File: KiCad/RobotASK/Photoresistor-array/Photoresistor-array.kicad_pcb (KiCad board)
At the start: 2 copper layers, 100 x 15 mm, 10 parts, among them J1 Conn_01x04_Pin, J2 Conn_01x02_Pin

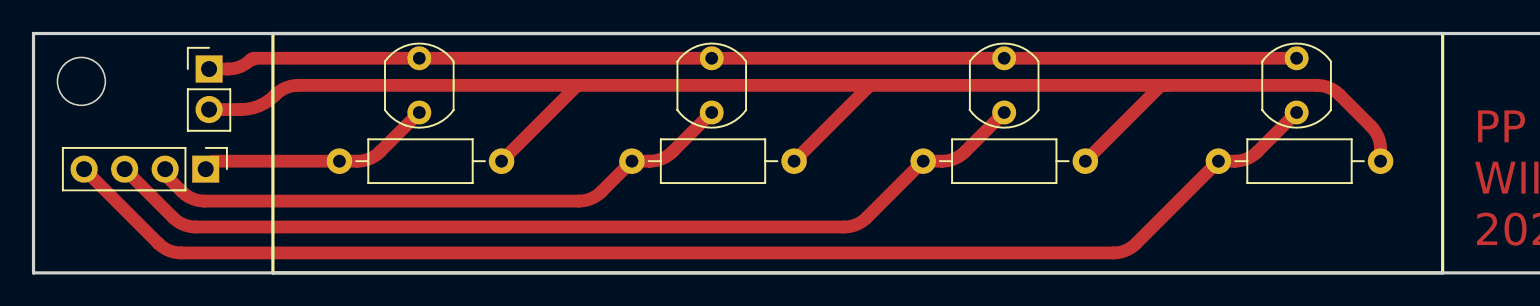
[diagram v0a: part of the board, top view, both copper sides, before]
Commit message: Edit pcb layers
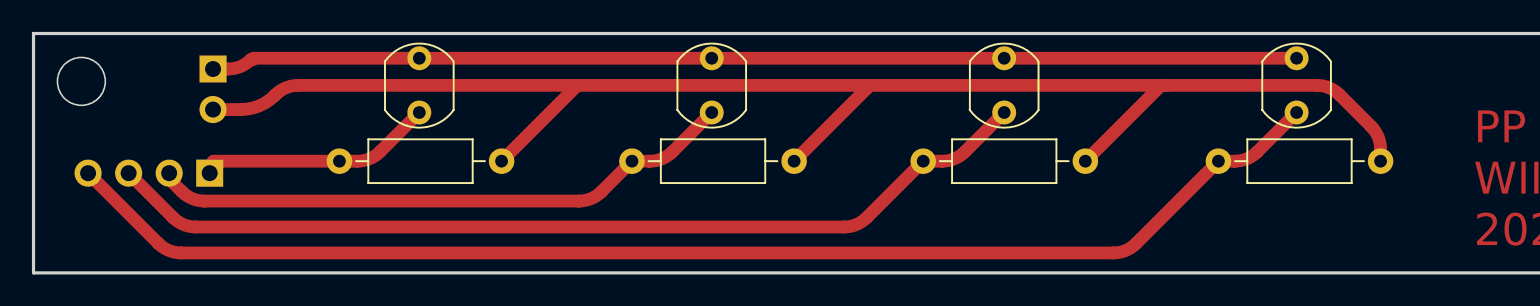
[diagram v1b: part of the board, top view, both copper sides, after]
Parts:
- J1, J2: moved to B.Cu
- moved J1 0.35 mm to (96.0, 58.8), turned to 90 degrees
- moved J2 0.25 mm to (96.2, 52.2), turned to 180 degrees

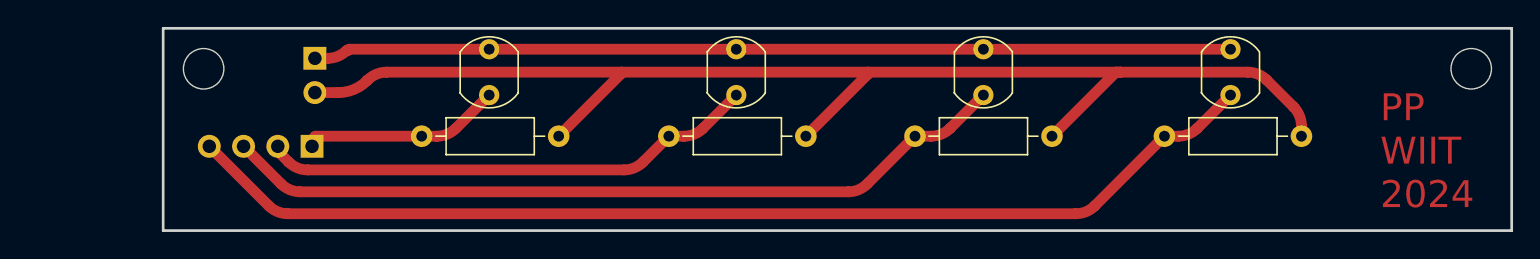
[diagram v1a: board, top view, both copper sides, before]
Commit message: Płytka fotorezystorów przedłużona aby piny były na dole
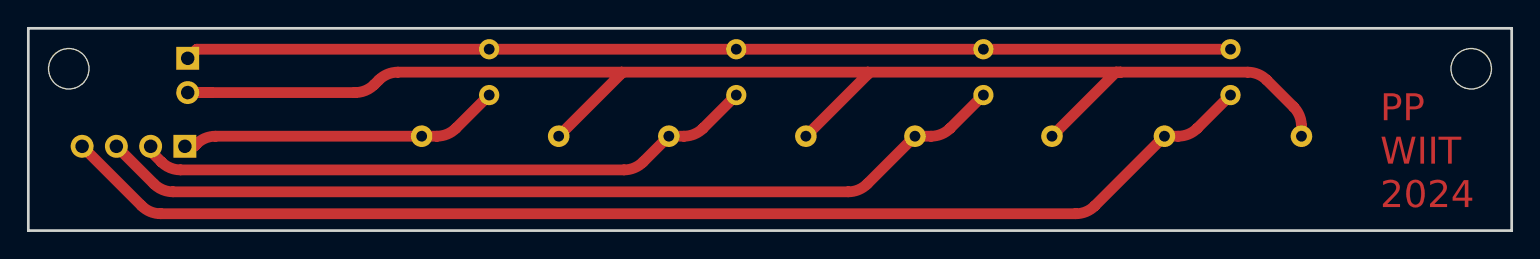
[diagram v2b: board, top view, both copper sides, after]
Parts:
- R1, R2, R3, R4, R5, R6, R7, R8: moved to B.Cu
- moved J1 9.43 mm to (86.6, 58.8)
- moved J2 9.43 mm to (86.8, 52.2)
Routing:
- net GND: track 96.9 -> 108.1 mm
- net PH1: track 37.3 -> 46.7 mm
- net PH2: track 59.3 -> 68.7 mm
- net PH3: track 81.5 -> 90.9 mm
- net +5V: track 68.3 -> 77.6 mm
- net PH0: track 14.8 -> 23.9 mm
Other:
- board size 100 x 15 mm -> 110 x 15 mm

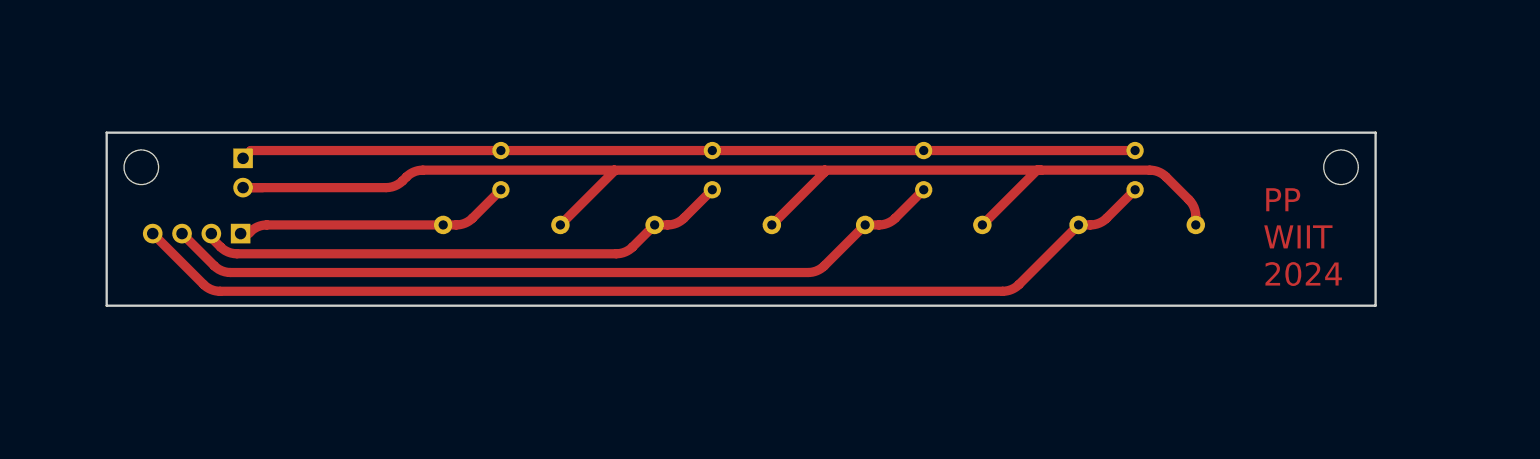
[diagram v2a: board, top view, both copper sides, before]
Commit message: Widen all possible traces, fill edge cuts layer, widen photoresistor PCB by 2mm
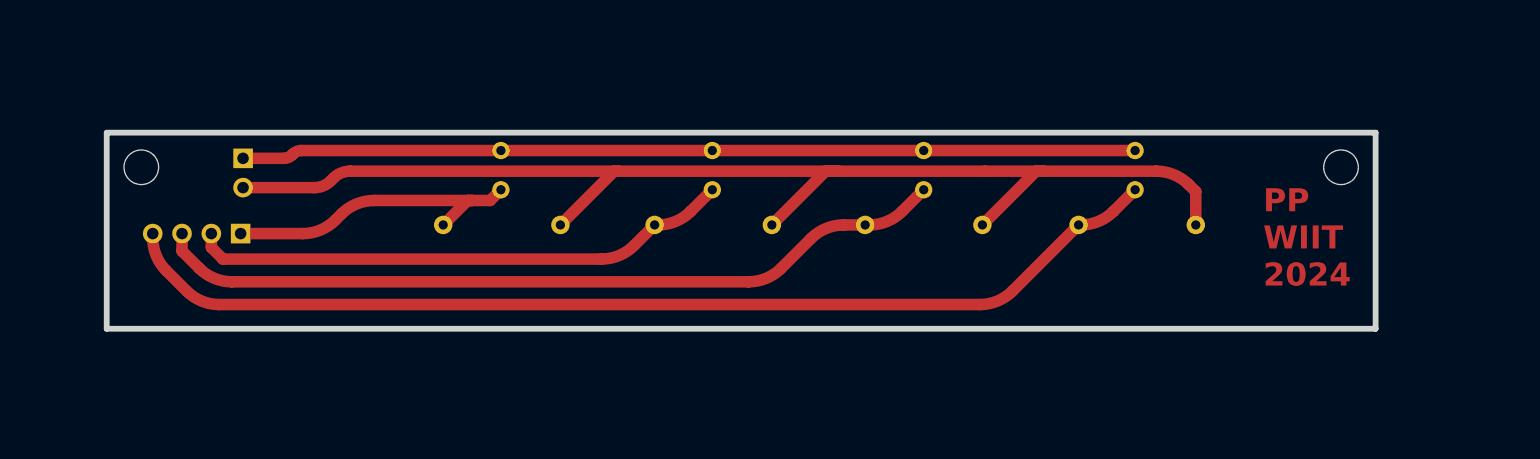
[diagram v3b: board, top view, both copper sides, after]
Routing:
- net PH0: track 23.9 -> 27.1 mm
- net PH3: track 90.9 -> 92.3 mm
- net PH2: track 68.7 -> 69.4 mm
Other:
- board size 110 x 15 mm -> 110 x 17 mm

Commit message: Poprawki kodu, zwiększenie otworów na komponenty na 1mm, nowe wydruki do termotransferu i nawiercania otworów, poukładanie nieaktualnych wydruków UV
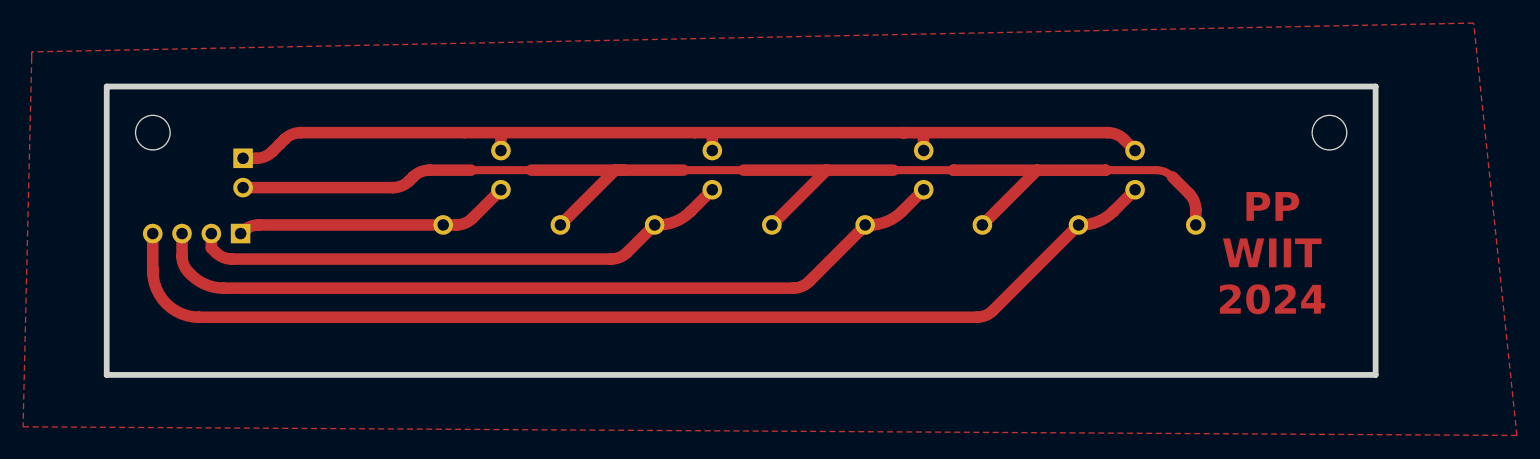
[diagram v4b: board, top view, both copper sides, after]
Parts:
- R1, R2, R3, R4: footprint Resistor_THT:R_Axial_DIN0207_L6.3mm_D2.5mm_P10.16mm_Horizontal -> Library:R_Axial_DIN0207_L6.3mm_D2.5mm_P10.16mm_Horizontal
- R5, R6, R7, R8: footprint OptoDevice:R_LDR_5.1x4.3mm_P3.4mm_Vertical -> Library:R_LDR_5.1x4.3mm_P3.4mm_Vertical
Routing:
- net +5V: track 77.5 -> 83.6 mm
- net PH0: track 27.1 -> 23.9 mm
- net PH3: track 92.3 -> 95.2 mm
- net PH2: track 69.4 -> 71.7 mm
- net GND: track 107.9 -> 106.9 mm
- added copper zone on F.Cu, net GND
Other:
- board size 110 x 17 mm -> 110 x 25 mm

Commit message: renders
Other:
- board text added: "+5V"
- board text added: "GND"
- board text added: "P0"
- board text added: "P1"
- board text added: "P2"
- board text added: "P3"
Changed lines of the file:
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@@
 		(0 "F.Cu" signal)
 		(31 "B.Cu" signal)
+		(36 "B.SilkS" user "B.Silkscreen")
 		(41 "Cmts.User" user "User.Comments")
 		(44 "Edge.Cuts" user)
@@
 			(layer "dielectric 1"
 				(type "prepreg")
-				(thickness 1)
+				(color "#633C00F2")
+				(thickness 1 locked)
 				(material "FR4")
 				(epsilon_r 4.5)
@@
 				(thickness 0.035)
 			)
+			(layer "B.SilkS"
+				(type "Bottom Silk Screen")
+				(color "White")
+				(material "Direct Printing")
+			)
 			(copper_finish "None")
 			(dielectric_constraints no)
@@
 		(pcbplotparams
 			(layerselection 0x0000000_7fffffff)
-			(plot_on_all_layers_selection 0x0001000_00000000)
+			(plot_on_all_layers_selection 0x003f210_80000001)
 			(disableapertmacros no)
 			(usegerberextensions no)
@@
 			(dashed_line_gap_ratio 3.000000)
 			(svgprecision 6)
-			(plotframeref no)
+			(plotframeref yes)
 			(viasonmask no)
 			(mode 1)
@@
 			(drillshape 2)
 			(scaleselection 1)
-			(outputdirectory "../../../wydruki/wiercenia/")
+			(outputdirectory "../../../../Pobrane/")
 		)
 	)
@@
 		(tags "Resistor Axial_DIN0207 series Axial Horizontal pin pitch 10.16mm 0.25W = 1/4W length 6.3mm diameter 2.5mm")
 		(property "Reference" "R4"
-			(at 5.08 2.37 180)
+			(at 2.76 -2.35 180)
 			(layer "B.SilkS")
 			(effects
@@
 		)
 		(property "Value" "10k"
-			(at 5.08 -2.37 180)
+			(at 7.26 -2.35 180)
 			(layer "B.Fab")
 			(effects
@@
 		(tags "Resistor Axial_DIN0207 series Axial Horizontal pin pitch 10.16mm 0.25W = 1/4W length 6.3mm diameter 2.5mm")
 		(property "Reference" "R1"
-			(at 5.08 2.37 180)
+			(at 2.78 -2.35 180)
 			(layer "B.SilkS")
 			(effects
@@
 		)
 		(property "Value" "10k"
-			(at 5.08 -2.37 180)
+			(at 7.28 -2.3 180)
 			(layer "B.Fab")
 			(effects
@@
 		(tags "Resistor Axial_DIN0207 series Axial Horizontal pin pitch 10.16mm 0.25W = 1/4W length 6.3mm diameter 2.5mm")
 		(property "Reference" "R2"
-			(at 5.08 2.37 180)
+			(at 2.71 -2.3 180)
 			(layer "B.SilkS")
 			(effects
@@
 		)
 		(property "Value" "10k"
-			(at 5.08 -2.37 180)
+			(at 7.06 -2.3 180)
 			(layer "B.Fab")
 			(effects
@@
 		(tags "Resistor Axial_DIN0207 series Axial Horizontal pin pitch 10.16mm 0.25W = 1/4W length 6.3mm diameter 2.5mm")
 		(property "Reference" "R3"
-			(at 5.08 2.37 180)
+			(at 2.71 -2.25 180)
 			(layer "B.SilkS")
 			(effects
@@
 		)
 		(property "Value" "10k"
-			(at 5.08 -2.37 180)
+			(at 7.11 -2.3 180)
 			(layer "B.Fab")
 			(effects
@@
 		)
 	)
+	(gr_text "P3"
+		(at 160.4 53.9 0)
+		(layer "B.SilkS")
+		(effects
+			(font
+				(size 1 1)
+				(thickness 0.15)
+			)
+			(justify left bottom mirror)
+		)
+	)
+	(gr_text "GND"
+		(at 92.2 55.55 0)
+		(layer "B.SilkS")
+		(effects
+			(font
+				(size 1 1)
+				(thickness 0.15)
+			)
+			(justify left bottom mirror)
+		)
+	)
+	(gr_text "+5V"
+		(at 92.2 52.7 0)
+		(layer "B.SilkS")
+		(effects
+			(font
+				(size 1 1)
+				(thickness 0.15)
+			)
+			(justify left bottom mirror)
+		)
+	)
+	(gr_text "P2"
+		(at 141.7 53.85 0)
+		(layer "B.SilkS")
+		(effects
+			(font
+				(size 1 1)
+				(thickness 0.15)
+			)
+			(justify left bottom mirror)
+		)
+	)
+	(gr_text "P1"
+		(at 85.033332 61.7 0)
+		(layer "B.SilkS")
+		(effects
+			(font
+				(size 1 1)
+				(thickness 0.15)
+			)
+			(justify left bottom mirror)
+		)
+	)
+	(gr_text "P0"
+		(at 105 53.9 0)
+		(layer "B.SilkS")
+		(effects
+			(font
+				(size 1 1)
+				(thickness 0.15)
+			)
+			(justify left bottom mirror)
+		)
+	)
+	(gr_text "P1"
+		(at 123.2 53.9 0)
+		(layer "B.SilkS")
+		(effects
+			(font
+				(size 1 1)
+				(thickness 0.15)
+			)
+			(justify left bottom mirror)
+		)
+	)
+	(gr_text "P3"
+		(at 79.8 61.7 0)
+		(layer "B.SilkS")
+		(effects
+			(font
+				(size 1 1)
+				(thickness 0.15)
+			)
+			(justify left bottom mirror)
+		)
+	)
+	(gr_text "P0"
+		(at 87.65 61.7 0)
+		(layer "B.SilkS")
+		(effects
+			(font
+				(size 1 1)
+				(thickness 0.15)
+			)
+			(justify left bottom mirror)
+		)
+	)
+	(gr_text "P2"
+		(at 82.416666 61.7 0)
+		(layer "B.SilkS")
+		(effects
+			(font
+				(size 1 1)
+				(thickness 0.15)
+			)
+			(justify left bottom mirror)
+		)
+	)
